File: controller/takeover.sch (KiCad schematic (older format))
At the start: 62 parts, among them J1 CONN_01X10, J2 CONN_01X10, J3 CONN_01X10, J4 CONN_01X10, K1 RELAY_SEPARATED, K10 RELAY_SEPARATED, K11 RELAY_SEPARATED, K12 RELAY_SEPARATED, K13 RELAY_SEPARATED, K14 RELAY_SEPARATED, K15 RELAY_SEPARATED, K16 RELAY_SEPARATED, K2 RELAY_SEPARATED, K3 RELAY_SEPARATED, K4 RELAY_SEPARATED, K5 RELAY_SEPARATED, K6 RELAY_SEPARATED, K7 RELAY_SEPARATED, K8 RELAY_SEPARATED, K9 RELAY_SEPARATED, U2 ULN2801A, U6 ULN2801A

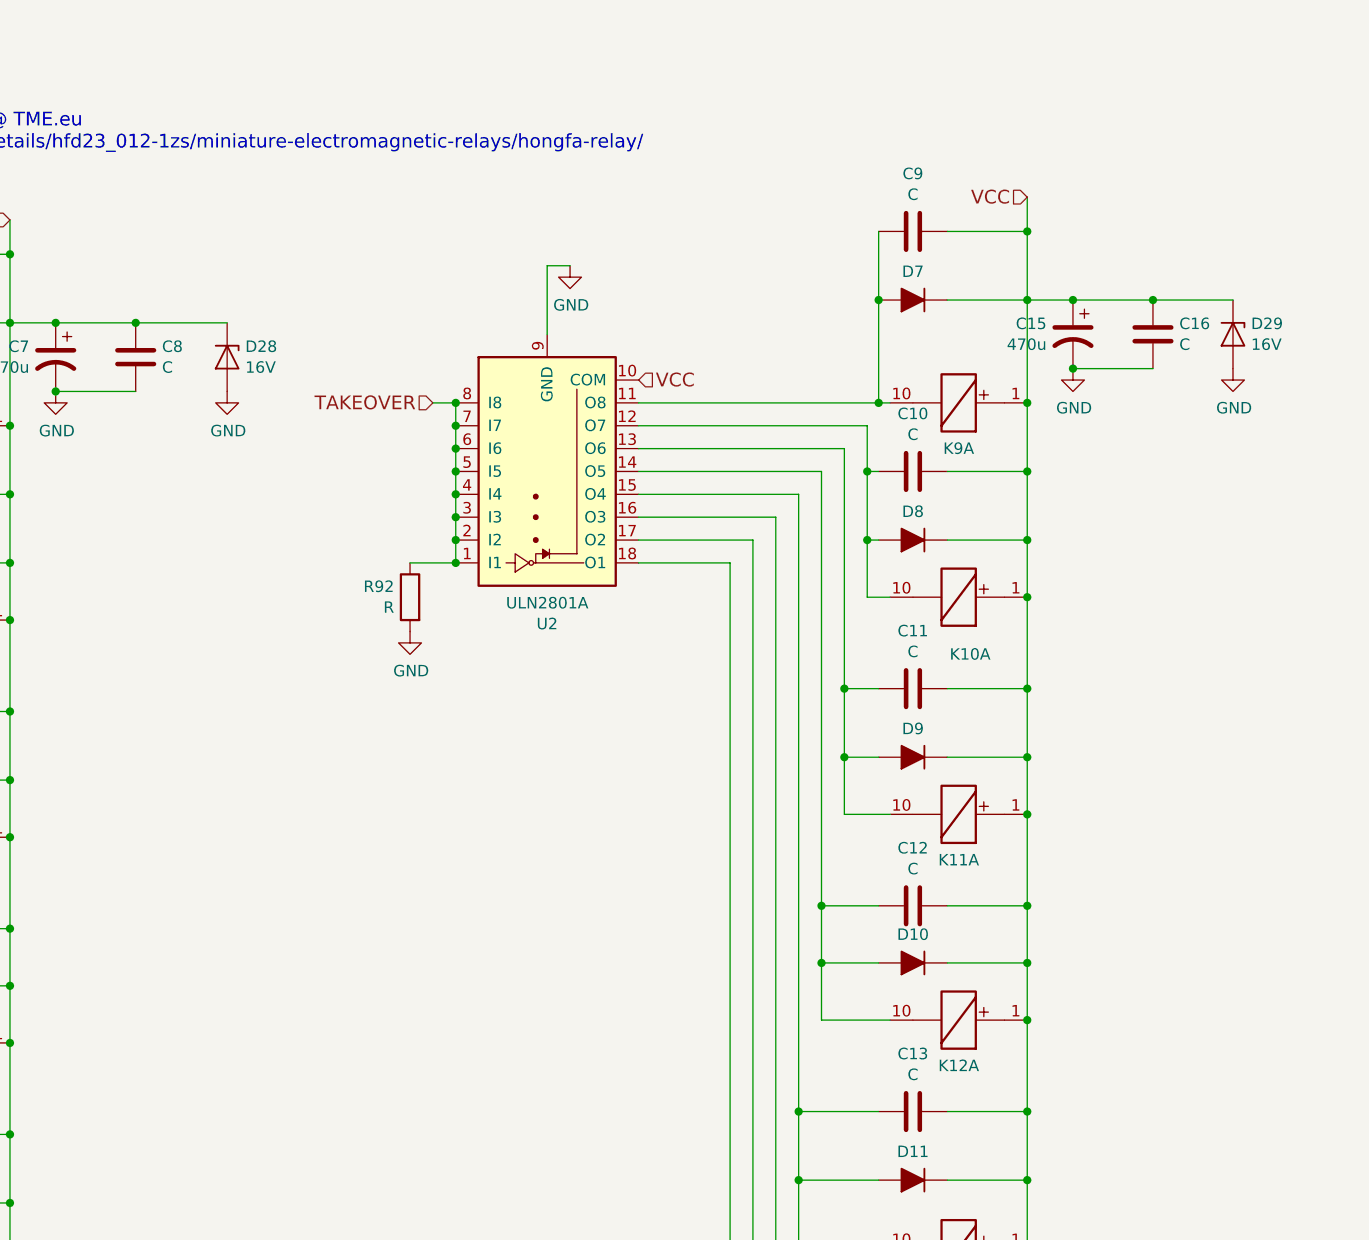
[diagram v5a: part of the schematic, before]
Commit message: Finish the routing, add some significant fixes: *correct to-252 pin numbering * longer pads for relays * fix footprint of the optocouplers
Also finish the routing
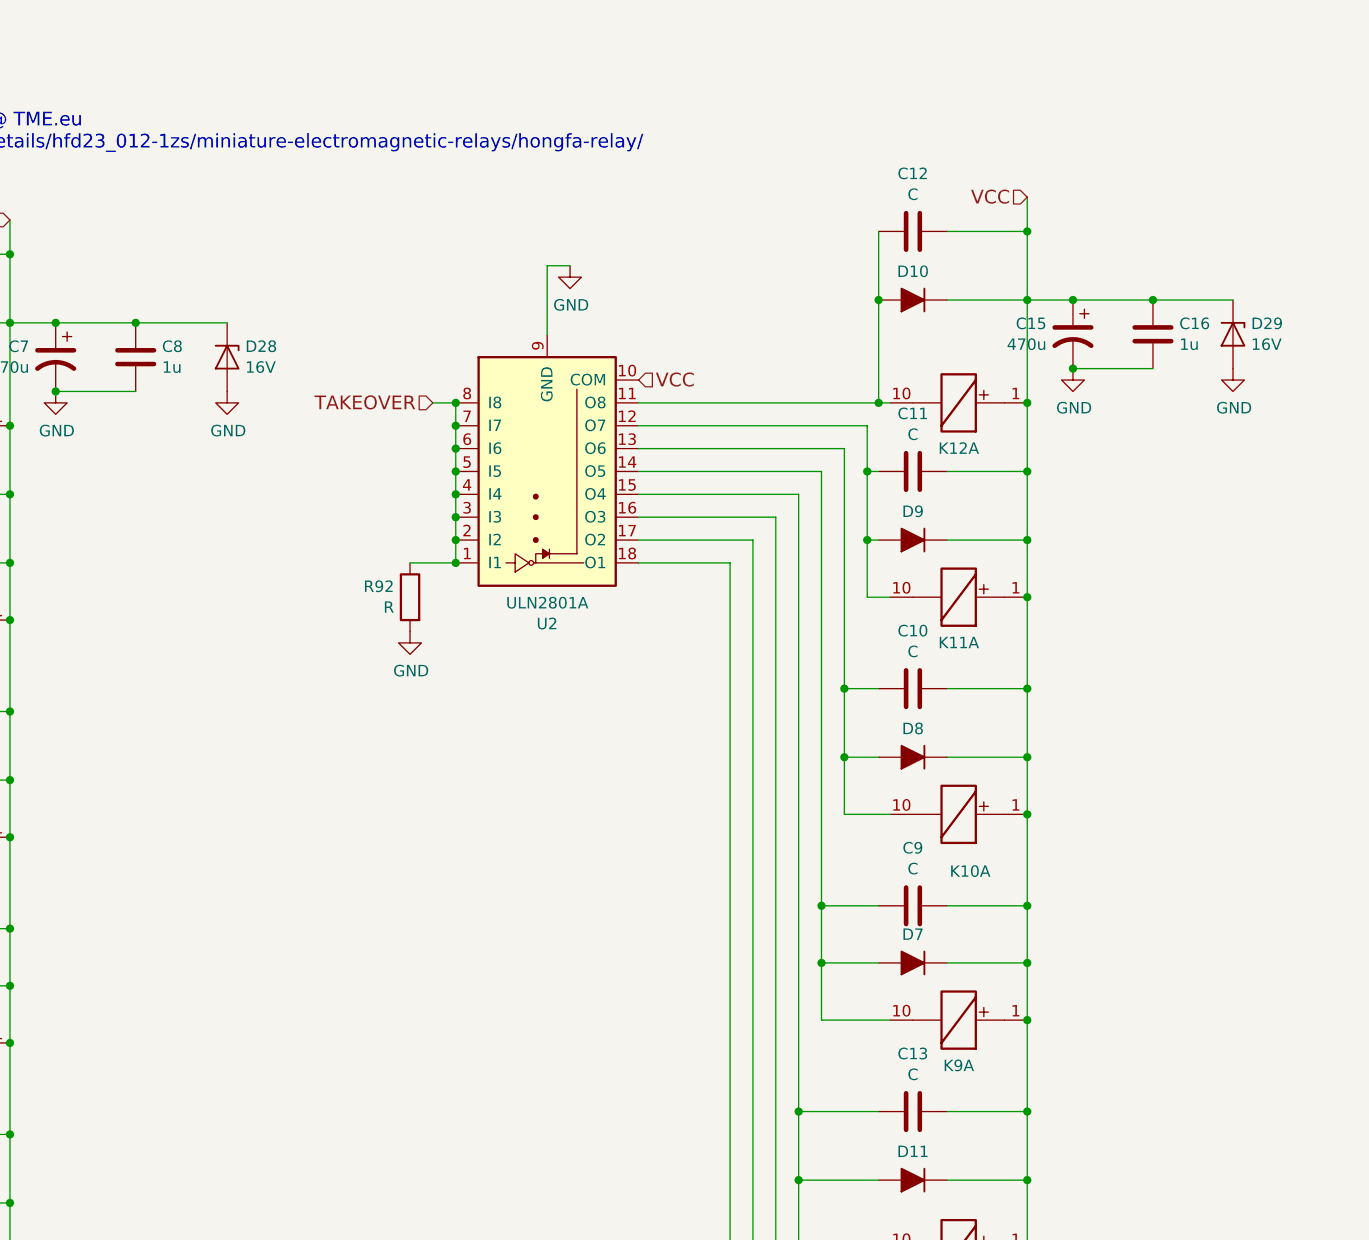
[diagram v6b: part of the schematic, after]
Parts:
- C16, C8: value C -> 1u; Distributor ? -> 2320928
- J1, J2, J3, J4: footprint Connectors_Terminal_Blocks:TerminalBlock_Pheonix_MKDS1.5-10pol -> smalsiukas-footpints:TerminalBlock_5.08-10pol
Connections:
- net at C10.2, D8.2 (A), K10.10: now also U2.13 (O6); no longer U2.12 (O7)
- net at C9.2, D7.2 (A), K9.10: now also U2.14 (O5); no longer U2.11 (O8)
- net at C11.2, D9.2 (A), K11.10: now also U2.12 (O7); no longer U2.13 (O6)
- net at C12.2, D10.2 (A), K12.10: now also U2.11 (O8); no longer U2.14 (O5)
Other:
- moved on the sheet: C10, C11, C12, C9, D10, D7, D8, D9, K10A, K11A, K12A, K9A
